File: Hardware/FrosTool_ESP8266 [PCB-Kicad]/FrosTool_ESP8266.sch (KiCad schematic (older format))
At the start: 1 part

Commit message: Added Schematic: libraries, power and sensors
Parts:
- added C?: 100nF, symbol C_Small
- added C?: 10uF, symbol CP
- added J?: Power_IN, symbol Conn_01x02
- added J?: UART, symbol Conn_01x02
- added J? (x2): DATA_S1, symbol Conn_01x01
- added J? (x2): Power_OUT, symbol Conn_01x02
- added J?: Debug, symbol Conn_01x01
- added U?: AP1117-33, TO_SOT_Packages_SMD:SOT-223-3Lead_TabPin2, symbol AP1117-33
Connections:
- net labels added: +3.3V, ADC_BAT, BAT+, DATA_S1, DATA_S2, GND
- wire segments 0 -> 27
- no-connect marks 0 -> 12
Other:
- note added: "ADC -> GPIO4"
- note added: "GPIO16 -> Deep-sleep mode"
- note added: "MODO PROGRAMACION"
- note added: "POWER IN [Vin: 5.3V -> Vout 3.3V]"
- note added: "SENSOR 1"
- note added: "SENSOR 2"
- note added: "SENSOR ANALOG -> GPIO"
- note added: "TODO"
- note added: "VOLATGE DIVISOR"
- moved on the sheet: U?

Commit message: Add sistema de carga al esquematico
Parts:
- removed J?: Power_IN, symbol Conn_01x02
- removed J?: UART, symbol Conn_01x02
- removed J?: Debug, symbol Conn_01x01
- added D? (x3): LED, symbol LED
- added J?: USB_OTG, symbol USB_OTG
- added J?: IN_PANEL, symbol CONN_01X02
- added J?: BATERIA, symbol CONN_01X02
- added Q? (x3): 2N3904, TO_SOT_Packages_THT:TO-92_Molded_Narrow, symbol 2N3904
- added R? (x6): R, symbol R
- added U?: CARGADOR, symbol CARGADOR
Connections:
- net labels added: CONEXION, LED1, LED2, RXD, TXD, V5
- wire segments 27 -> 57

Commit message: Added sheet Linear Li-lon Battery Charger
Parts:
- removed J? (x2): Power_OUT, symbol Conn_01x02
- added J? (x2): GND, symbol Conn_01x01
- added J? (x2): V3.3, symbol Conn_01x01
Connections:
- net +3V3: now also J?.1 (Pin_1), J?.1 (Pin_1)
- net GND: now also J?.1 (Pin_1), J?.1 (Pin_1)
- net CONEXION renamed DEBUG_LED
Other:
- note added: "ESP8266"
- moved on the sheet: D?, J?, Q?, R?

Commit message: ESP8266 Mod Prog
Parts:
- removed J?: USB_OTG, symbol USB_OTG
- added J?: TX_RX, symbol Conn_01x02
- added R? (x2): 4.7k, symbol R
- added SW?: Flash, symbol SW_Push
- added SW?: Reset, symbol SW_Push
- R?: value R -> 1k
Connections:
- net +3V3: now also R?.1, R?.2
- net DATA_S2: no longer U?.12 (GPIO0)
- net GND: now also SW?.2, SW?.2
- net RXD: now also J?.2 (Pin_2)
- net TXD: now also J?.1 (Pin_1)
- net at U?.1 (REST): now also R?.1, SW?.1
- net V5: no longer names the net of J?.2 (P2), U?.1 (P+)
- new net: R?.2, SW?.1, U?.12 (GPIO0)
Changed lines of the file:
@@
 LIBS:ESP8266
 LIBS:tp4056
+LIBS:switches
 LIBS:FrosTool_ESP8266-cache
 EELAYER 25 0
@@
 Text Notes 1000 6550 0    60   ~ 0
 ADC -> GPIO4
-$Comp
-L +3.3V #PWR?
-U 1 1 59D48315
-P 4100 3550
-F 0 "#PWR?" H 4100 3400 50  0001 C CNN
-F 1 "+3.3V" H 4000 3700 50  0000 C CNN
-F 2 "" H 4100 3550 50  0001 C CNN
-F 3 "" H 4100 3550 50  0001 C CNN
-	1    4100 3550
-	0    -1   -1   0
-$EndComp
 Text Label 6050 3650 0    60   ~ 0
 ADC_BAT
 Text Label -850 5200 0    60   ~ 0
 ADC_BAT
-Text Label 6050 3750 0    60   ~ 0
+Text Label 8100 4400 0    60   ~ 0
 DATA_S2
 Text Label -2450 5200 2    60   ~ 0
@@
 NoConn ~ 5350 4550
 $Comp
-L USB_OTG J?
-U 1 1 59D7F39A
-P 13400 1700
-F 0 "J?" H 13455 2167 50  0000 C CNN
-F 1 "USB_OTG" H 13455 2076 50  0000 C CNN
-F 2 "" H 13550 1650 50  0001 C CNN
-F 3 "" H 13550 1650 50  0001 C CNN
-	1    13400 1700
-	1    0    0    -1
-$EndComp
-$Comp
-L GND #PWR?
-U 1 1 59D7F4E3
-P 13400 2250
-F 0 "#PWR?" H 13400 2000 50  0001 C CNN
-F 1 "GND" H 13405 2077 50  0000 C CNN
-F 2 "" H 13400 2250 50  0001 C CNN
-F 3 "" H 13400 2250 50  0001 C CNN
-	1    13400 2250
-	1    0    0    -1
-$EndComp
-Text GLabel 14000 1700 2    60   Input ~ 0
-TXD
-Text GLabel 14000 1800 2    60   Input ~ 0
-RXD
-Text GLabel 14000 1500 2    60   Input ~ 0
-V5
-$Comp
 L CONN_01X02 J?
 U 1 1 59D806A2
@@
 	-1   0    0    1
 $EndComp
-Text GLabel 1300 1200 1    60   Input ~ 0
-V5
 $Comp
 L CARGADOR U?
@@
 	9600 3500 9600 3650
 Wire Wire Line
-	2350 1600 2350 1700
+	2350 1600 2350 2000
 Wire Wire Line
 	3250 1700 3250 1800
@@
 	850  7600 850  6350
 Wire Wire Line
-	6050 3750 6000 3750
-Wire Wire Line
-	4200 3550 4100 3550
+	6000 3750 6650 3750
 Wire Wire Line
 	6050 3650 6000 3650
@@
 	1000 6950 1150 6950
 Wire Wire Line
-	13400 2250 13400 2100
-Wire Wire Line
-	14000 1800 13700 1800
-Wire Wire Line
-	13700 1700 14000 1700
-Wire Wire Line
-	13300 2100 13300 2150
-Wire Wire Line
-	13300 2150 13400 2150
-Connection ~ 13400 2150
-Wire Wire Line
-	14000 1500 13700 1500
-Wire Wire Line
 	2100 1400 2950 1400
 Wire Wire Line
@@
 Wire Wire Line
 	1150 1650 1150 1550
-Wire Wire Line
-	1300 1200 1300 1400
-Connection ~ 1300 1400
 Wire Wire Line
 	2550 1900 2550 1400
 Connection ~ 2550 1400
 Wire Wire Line
-	2550 2000 2400 2000
-Wire Wire Line
-	2400 2000 2400 1700
-Connection ~ 2400 1700
+	2350 2000 2550 2000
 Wire Wire Line
 	1850 1950 1850 1800
@@
 U 1 1 59D831EB
 P 6600 5650
-F 0 "R?" V 6393 5650 50  0000 C CNN
-F 1 "R" V 6484 5650 50  0000 C CNN
+F 0 "R?" V 6500 5650 50  0000 C CNN
+F 1 "1k" V 6600 5650 50  0000 C CNN
 F 2 "" V 6530 5650 50  0001 C CNN
 F 3 "" H 6600 5650 50  0001 C CNN
@@
 	9750 4700 9800 4700
 $Sheet
-S 1700 2750 550  450
+S 1600 2700 550  450
 U 59DAA3AB
 F0 "TP4056" 60
 F1 "TP4056.sch" 60
 $EndSheet
+$Comp
+L R R?
+U 1 1 59DAD4BD
+P 6800 3750
+F 0 "R?" V 6880 3750 50  0000 C CNN
+F 1 "4.7k" V 6800 3750 50  0000 C CNN
+F 2 "" V 6730 3750 50  0001 C CNN
+F 3 "" H 6800 3750 50  0001 C CNN
+	1    6800 3750
+	0    1    1    0
+$EndComp
+$Comp
+L +3.3V #PWR?
+U 1 1 59DADAE9
+P 7050 3750
+F 0 "#PWR?" H 7050 3600 50  0001 C CNN
+F 1 "+3.3V" H 7050 3890 50  0000 C CNN
+F 2 "" H 7050 3750 50  0001 C CNN
+F 3 "" H 7050 3750 50  0001 C CNN
+	1    7050 3750
+	0    1    1    0
+$EndComp
+$Comp
+L SW_Push SW?
+U 1 1 59DAE2D2
+P 6800 3500
+F 0 "SW?" H 6850 3600 50  0000 L CNN
+F 1 "Flash" H 6800 3440 50  0000 C CNN
+F 2 "" H 6800 3700 50  0001 C CNN
+F 3 "" H 6800 3700 50  0001 C CNN
+	1    6800 3500
+	1    0    0    -1
+$EndComp
+Wire Wire Line
+	6600 3500 6550 3500
+Wire Wire Line
+	6550 3500 6550 3750
+Connection ~ 6550 3750
+$Comp
+L GND #PWR?
+U 1 1 59DAE702
+P 7050 3500
+F 0 "#PWR?" H 7050 3250 50  0001 C CNN
+F 1 "GND" H 7050 3350 50  0000 C CNN
+F 2 "" H 7050 3500 50  0001 C CNN
+F 3 "" H 7050 3500 50  0001 C CNN
+	1    7050 3500
+	0    -1   -1   0
+$EndComp
+Wire Wire Line
+	7050 3500 7000 3500
+$Comp
+L SW_Push SW?
+U 1 1 59DAE930
+P 3800 2900
+F 0 "SW?" H 3850 3000 50  0000 L CNN
+F 1 "Reset" H 3800 2840 50  0000 C CNN
+F 2 "" H 3800 3100 50  0001 C CNN
+F 3 "" H 3800 3100 50  0001 C CNN
+	1    3800 2900
+	0    -1   -1   0
+$EndComp
+$Comp
+L R R?
+U 1 1 59DAED0B
+P 3600 2900
+F 0 "R?" V 3680 2900 50  0000 C CNN
+F 1 "4.7k" V 3600 2900 50  0000 C CNN
+F 2 "" V 3530 2900 50  0001 C CNN
+F 3 "" H 3600 2900 50  0001 C CNN
+	1    3600 2900
+	-1   0    0    1
+$EndComp
+Wire Wire Line
+	7050 3750 6950 3750
+$Comp
+L GND #PWR?
+U 1 1 59DB1839
+P 3800 2600
+F 0 "#PWR?" H 3800 2350 50  0001 C CNN
+F 1 "GND" H 3800 2450 50  0000 C CNN
+F 2 "" H 3800 2600 50  0001 C CNN
+F 3 "" H 3800 2600 50  0001 C CNN
+	1    3800 2600
+	-1   0    0    1
+$EndComp
+$Comp
+L +3.3V #PWR?
+U 1 1 59DB19A0
+P 3600 2600
+F 0 "#PWR?" H 3600 2450 50  0001 C CNN
+F 1 "+3.3V" H 3500 2750 50  0000 C CNN
+F 2 "" H 3600 2600 50  0001 C CNN
+F 3 "" H 3600 2600 50  0001 C CNN
+	1    3600 2600
+	1    0    0    -1
+$EndComp
+Wire Wire Line
+	3800 2600 3800 2700
+Wire Wire Line
+	3800 3350 3800 3100
+Wire Wire Line
+	3600 2750 3600 2600
+Wire Wire Line
+	3600 3050 3600 3200
+Wire Wire Line
+	3600 3200 3800 3200
+Connection ~ 3800 3200
+Wire Wire Line
+	4200 3350 3800 3350
+$Comp
+L +3.3V #PWR?
+U 1 1 59DB2842
+P 4000 3550
+F 0 "#PWR?" H 4000 3400 50  0001 C CNN
+F 1 "+3.3V" H 3900 3700 50  0000 C CNN
+F 2 "" H 4000 3550 50  0001 C CNN
+F 3 "" H 4000 3550 50  0001 C CNN
+	1    4000 3550
+	0    -1   -1   0
+$EndComp
+Wire Wire Line
+	4000 3550 4200 3550
+$Comp
+L Conn_01x02 J?
+U 1 1 59DB3C41
+P 6900 3100
+F 0 "J?" H 6900 3200 50  0000 C CNN
+F 1 "TX_RX" H 6900 2900 50  0000 C CNN
+F 2 "" H 6900 3100 50  0001 C CNN
+F 3 "" H 6900 3100 50  0001 C CNN
+	1    6900 3100
+	1    0    0    1
+$EndComp
+Text Label 6600 3100 2    60   ~ 0
+TXD
+Text Label 6600 3000 2    60   ~ 0
+RXD
+Wire Wire Line
+	6700 3000 6600 3000
+Wire Wire Line
+	6600 3100 6700 3100
 $EndSCHEMATC

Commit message: IO CONN
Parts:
- added J?: GPIO12(D/A), symbol Conn_01x01
- added J? (x3): GPIO13(D), symbol Conn_01x01
- added J?: GND, symbol Conn_01x01
- added J?: V3.3, symbol Conn_01x01
- added R?: 0, symbol R
- J?: value DATA_S1 -> GPIO14(D/A)
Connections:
- net DATA_S2 is gone; now on net GPIO14: J?.1 (Pin_1)
- net +3V3: now also J?.1 (Pin_1)
- net GND: now also J?.1 (Pin_1)
- net at R?.1, SW?.1, U?.1 (REST): now also R?.2
- net GPIO15: now reaches U?.10 (GPIO15)
- net GPIO15: now also J?.1 (Pin_1)
- net ADC: now reaches U?.2 (ADC)
- net at U?.4 (GPIO16): now also R?.1
- net GPIO14: now reaches U?.5 (GPIO14)
- net GPIO12: now reaches U?.6 (GPIO12)
- net GPIO12: now also J?.1 (Pin_1)
- net GPIO13: now reaches U?.7 (GPIO13)
- net GPIO13: now also J?.1 (Pin_1)
- net ADC_BAT renamed GPIO4
- net GPIO4: now also J?.1 (Pin_1)
- net DATA_S1 renamed GPIO5
- no-connect marks 12 -> 6
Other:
- note added: "GPIO16 -> Deep-sleep mode (Change Resistor)"
- note added: "IO CONN"
- note removed: "ADC -> GPIO4"
- note removed: "GPIO16 -> Deep-sleep mode"
- note removed: "MODO PROGRAMACION"
- note removed: "SENSOR 1"
- note removed: "SENSOR 2"
- note removed: "SENSOR ANALOG -> GPIO"
- note removed: "VOLATGE DIVISOR"
- moved on the sheet: D?, J?, Q?, R?

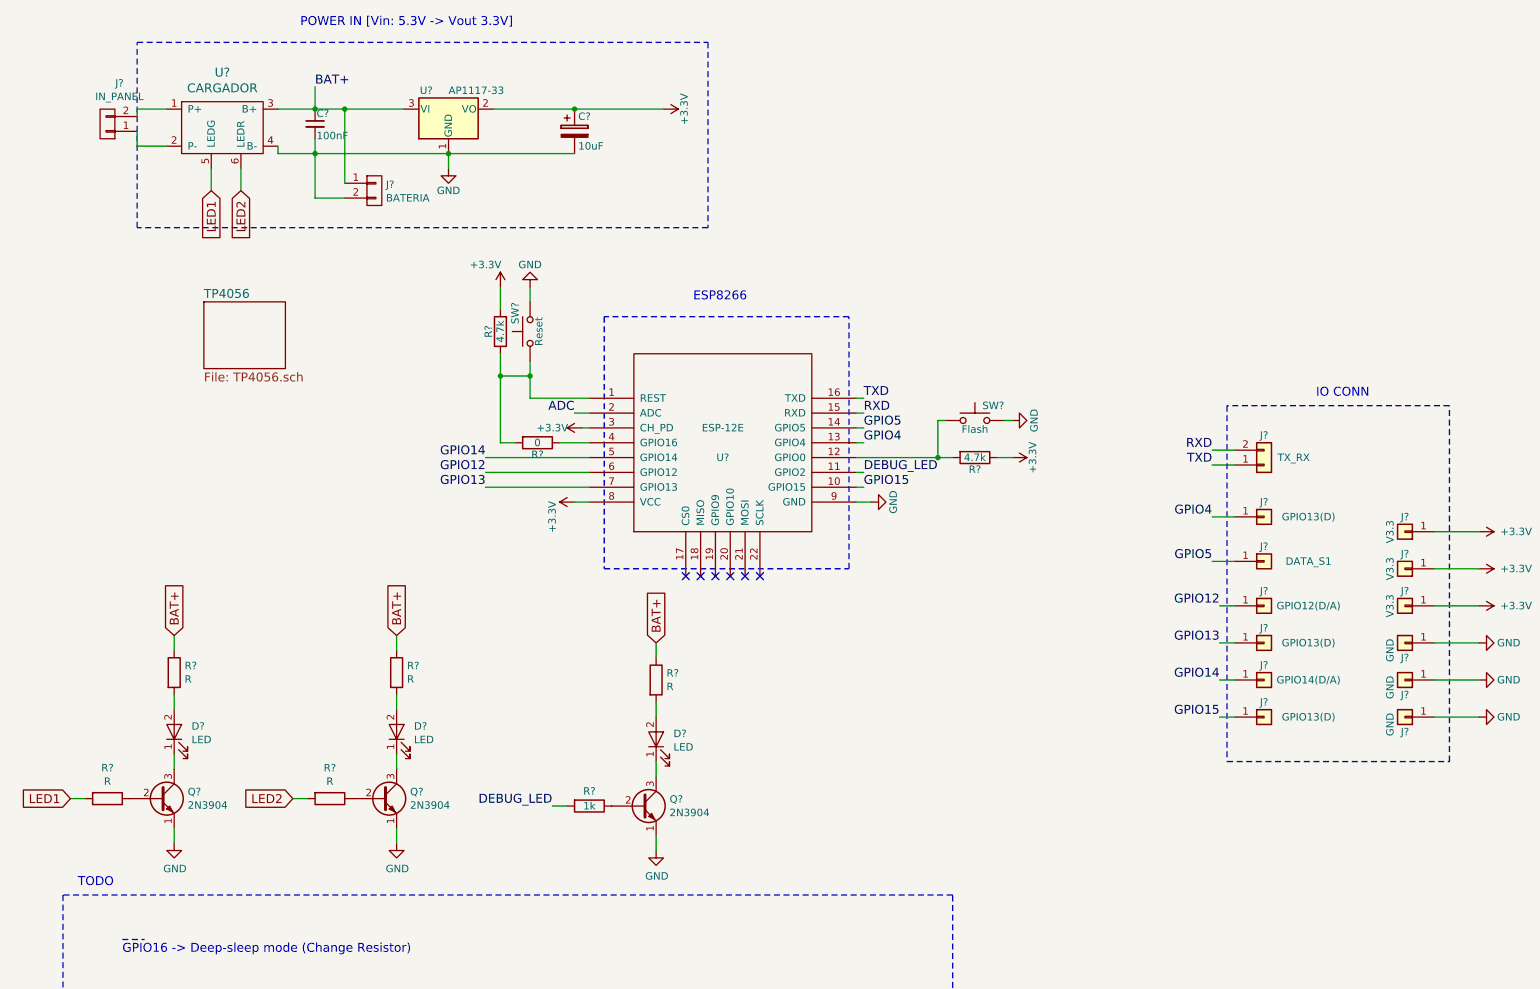
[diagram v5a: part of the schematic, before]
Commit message: Removed the old TP4056 component
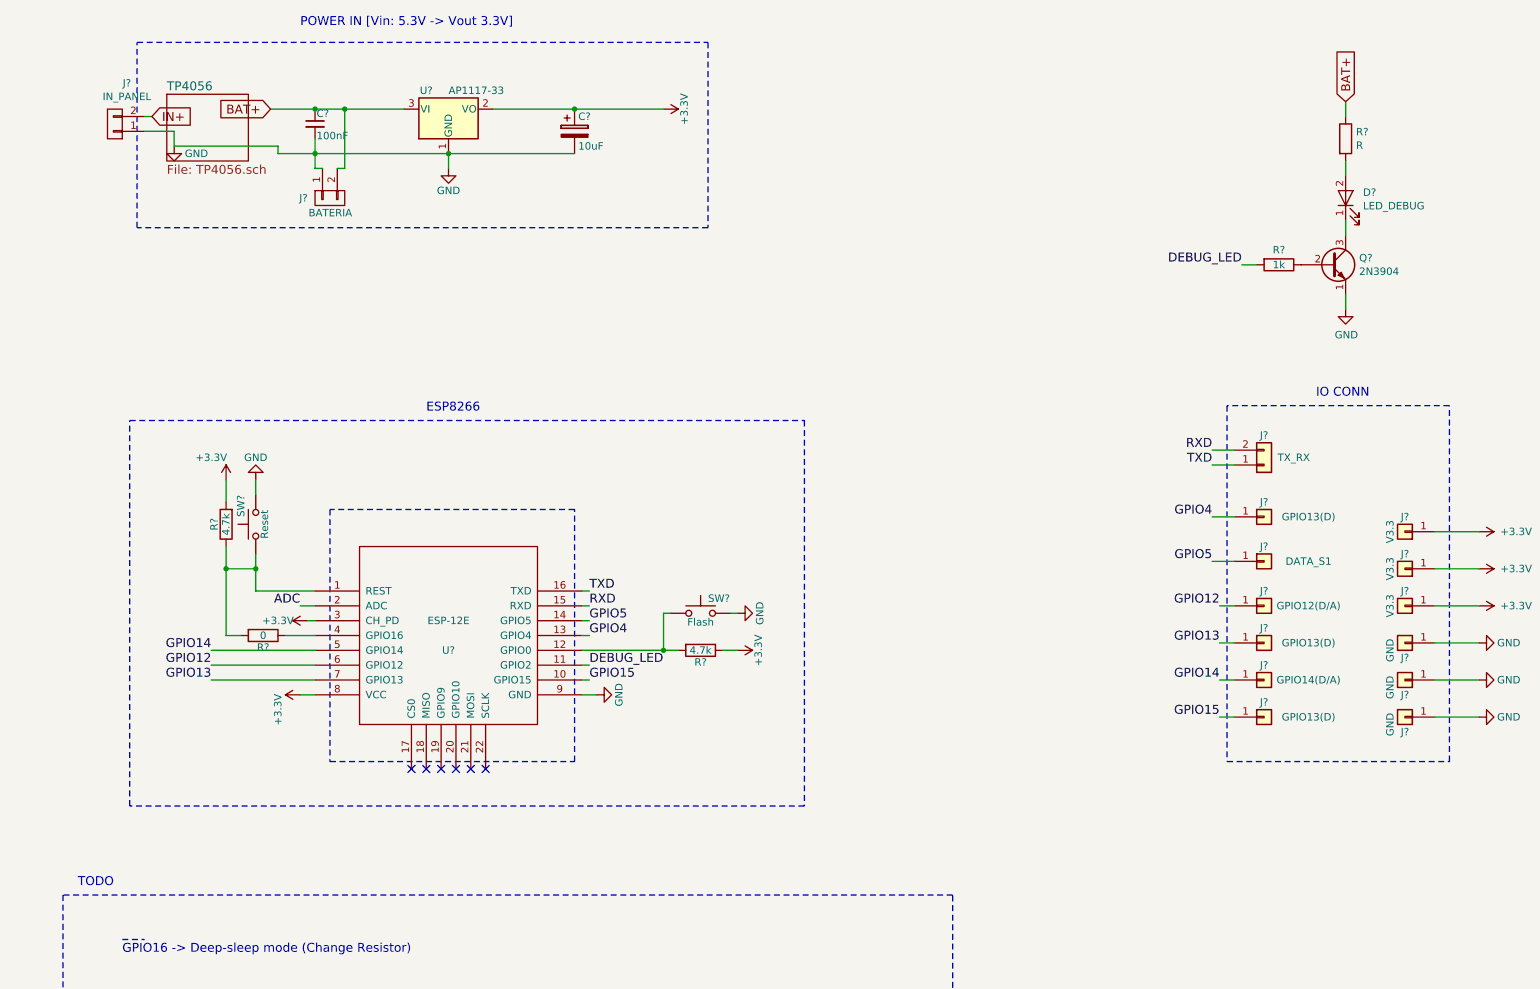
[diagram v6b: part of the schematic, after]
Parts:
- removed D? (x2): LED, symbol LED
- removed Q? (x2): 2N3904, TO_SOT_Packages_THT:TO-92_Molded_Narrow, symbol 2N3904
- removed R? (x4): R, symbol R
- removed U?: CARGADOR, symbol CARGADOR
- D?: value LED -> LED_DEBUG
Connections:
- net BAT+: now also J?.2 (P2); no longer J?.1 (P1)
- net GND: now also J?.1 (P1), J?.1 (P1); no longer J?.2 (P2)
- net IN+: now reaches J?.2 (P2)
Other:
- moved on the sheet: D?, J?, Q?, R?, SW?, U?

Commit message: Added NETList
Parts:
- gave numbers to parts that had none: 28

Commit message: Footprints
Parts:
- C1: footprint (none) -> Capacitors_SMD:C_0805
- C2: footprint (none) -> Capacitors_SMD:c_elec_3x5.3
- D1: footprint (none) -> LEDs:LED-3MM
- J1, J2, J3: footprint (none) -> Pin_Headers:Pin_Header_Straight_1x02_Pitch2.00mm
- J10, J11, J12, J13, J14, J15, J4, J5, J6, J7, J8, J9: footprint (none) -> Pin_Headers:Pin_Header_Straight_1x01
- Q1: footprint TO_SOT_Packages_THT:TO-92_Molded_Narrow -> TO_SOT_Packages_SMD:SOT-23
- R1, R2, R3, R4: footprint (none) -> Resistors_SMD:R_1206
- R5: value R -> 470; footprint (none) -> Resistors_SMD:R_1206
- SW1, SW2: footprint (none) -> Buttons_Switches_SMD:SW_SPST_B3U-1000P
- U1: footprint TO_SOT_Packages_SMD:SOT-223-3Lead_TabPin2 -> TO_SOT_Packages_SMD:SOT89-3_Housing
- U2: footprint (none) -> ESP8266:ESP-12E_SMD
